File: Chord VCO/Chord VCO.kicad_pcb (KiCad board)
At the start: 4 copper layers, 107 x 73 mm, 35 parts, among them J1 POWER/SIGNALS, J2 POTS/SWITCHES, U1 MOUDLE-SEEEDUINO-XIAO, U2 TL074

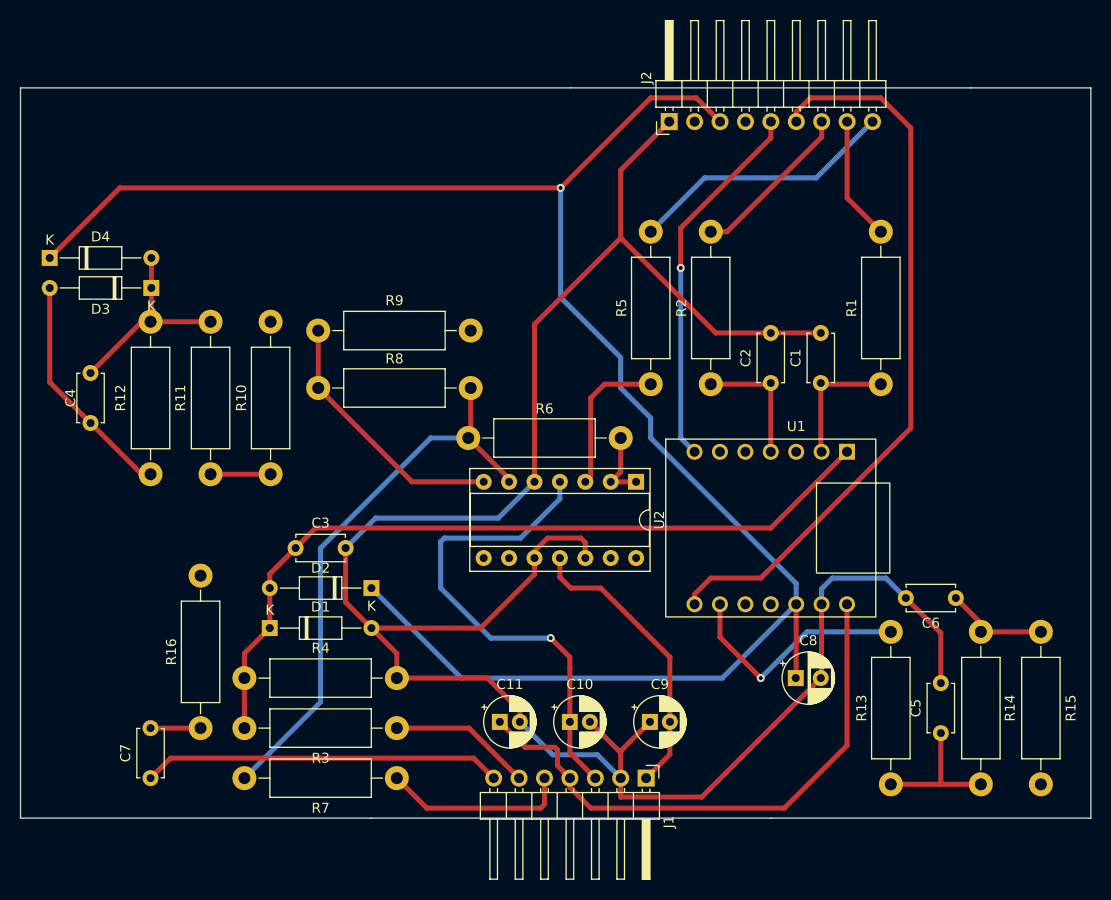
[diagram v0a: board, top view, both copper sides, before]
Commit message: Added fill zones to Chord VCO pcb
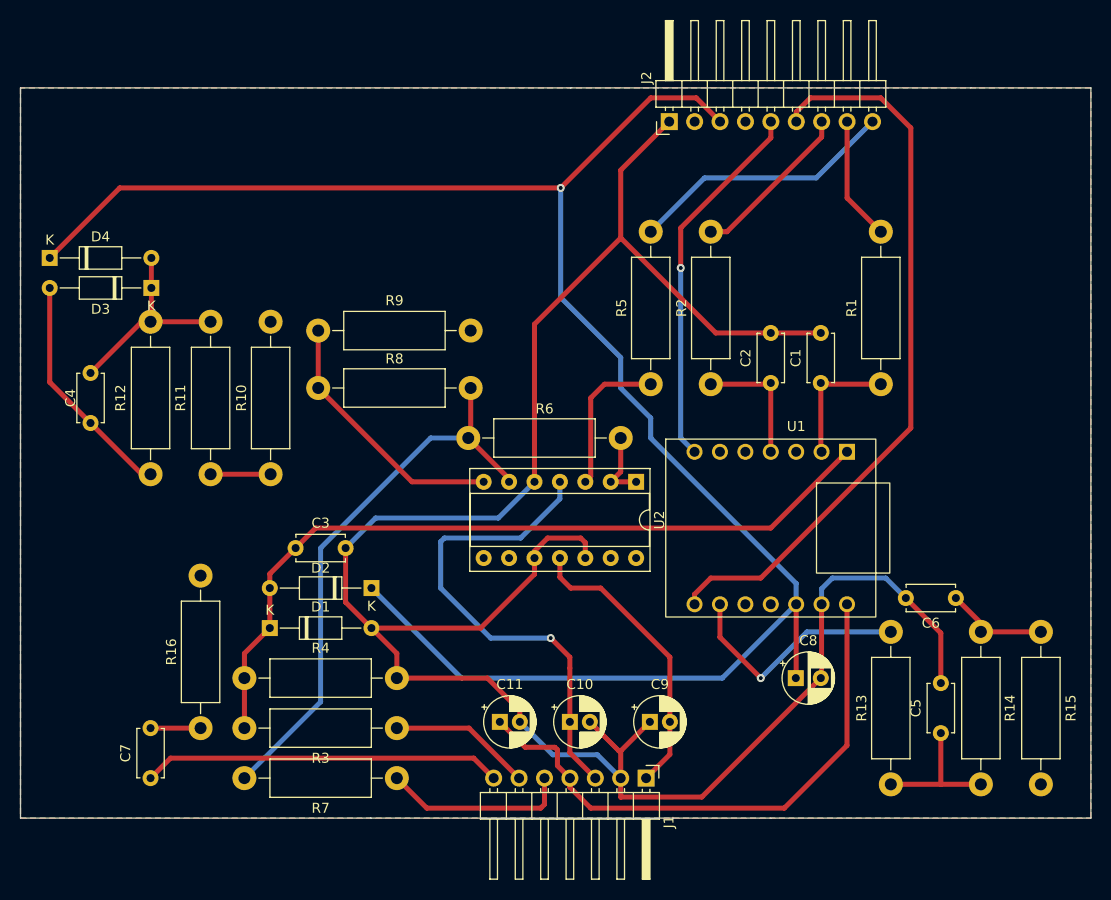
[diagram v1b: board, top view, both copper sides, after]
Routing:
- added copper zone on B.Cu, net (none)
- added copper zone on F.Cu, net (none)
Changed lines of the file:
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@@
   (segment (start 103.76 79) (end 123 79) (width 1) (layer "In1.Cu") (net 29))
   (segment (start 146.54 79.13137) (end 149 81.59137) (width 1) (layer "In1.Cu") (net 29))
+  (zone (net 0) (net_name "") (layer "F.Cu") (hatch edge 0.5)
+    (connect_pads (clearance 0.5))
+    (min_thickness 0.25) (filled_areas_thickness no)
+    (fill yes (thermal_gap 0.5) (thermal_bridge_width 0.5) (island_removal_mode 1) (island_area_min 10))
+    (polygon
+      (pts
+        (xy 85 31)
+        (xy 85 104)
+        (xy 192 104)
+        (xy 192 31)
+      )
+    )
+  )
+  (zone (net 0) (net_name "") (layer "B.Cu") (hatch edge 0.5)
+    (priority 1)
+    (connect_pads (clearance 0.5))
+    (min_thickness 0.25) (filled_areas_thickness no)
+    (fill yes (thermal_gap 0.5) (thermal_bridge_width 0.5) (island_removal_mode 1) (island_area_min 10))
+    (polygon
+      (pts
+        (xy 85 31)
+        (xy 85 104)
+        (xy 192 104)
+        (xy 192 31)
+      )
+    )
+  )
 )
